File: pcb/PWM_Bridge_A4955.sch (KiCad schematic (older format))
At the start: 18 parts, among them Q3 IPD079N06L3G, Q4 IPD079N06L3G, Q5 IPD079N06L3G, Q6 IPD079N06L3G, U5 A4955GLPTR-T

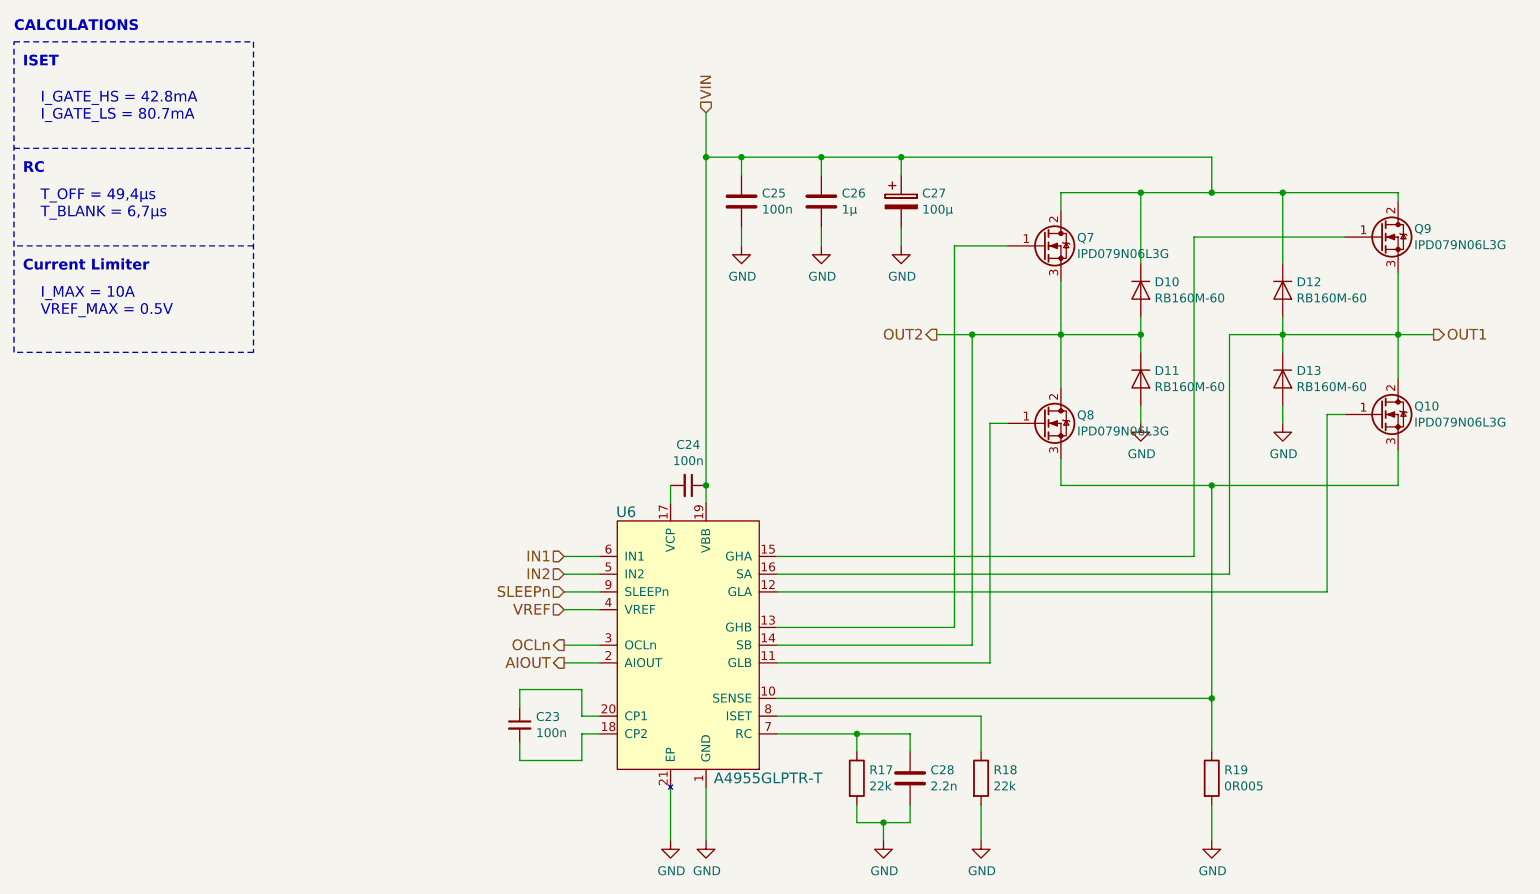
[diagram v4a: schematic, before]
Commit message: Fix little schematic error
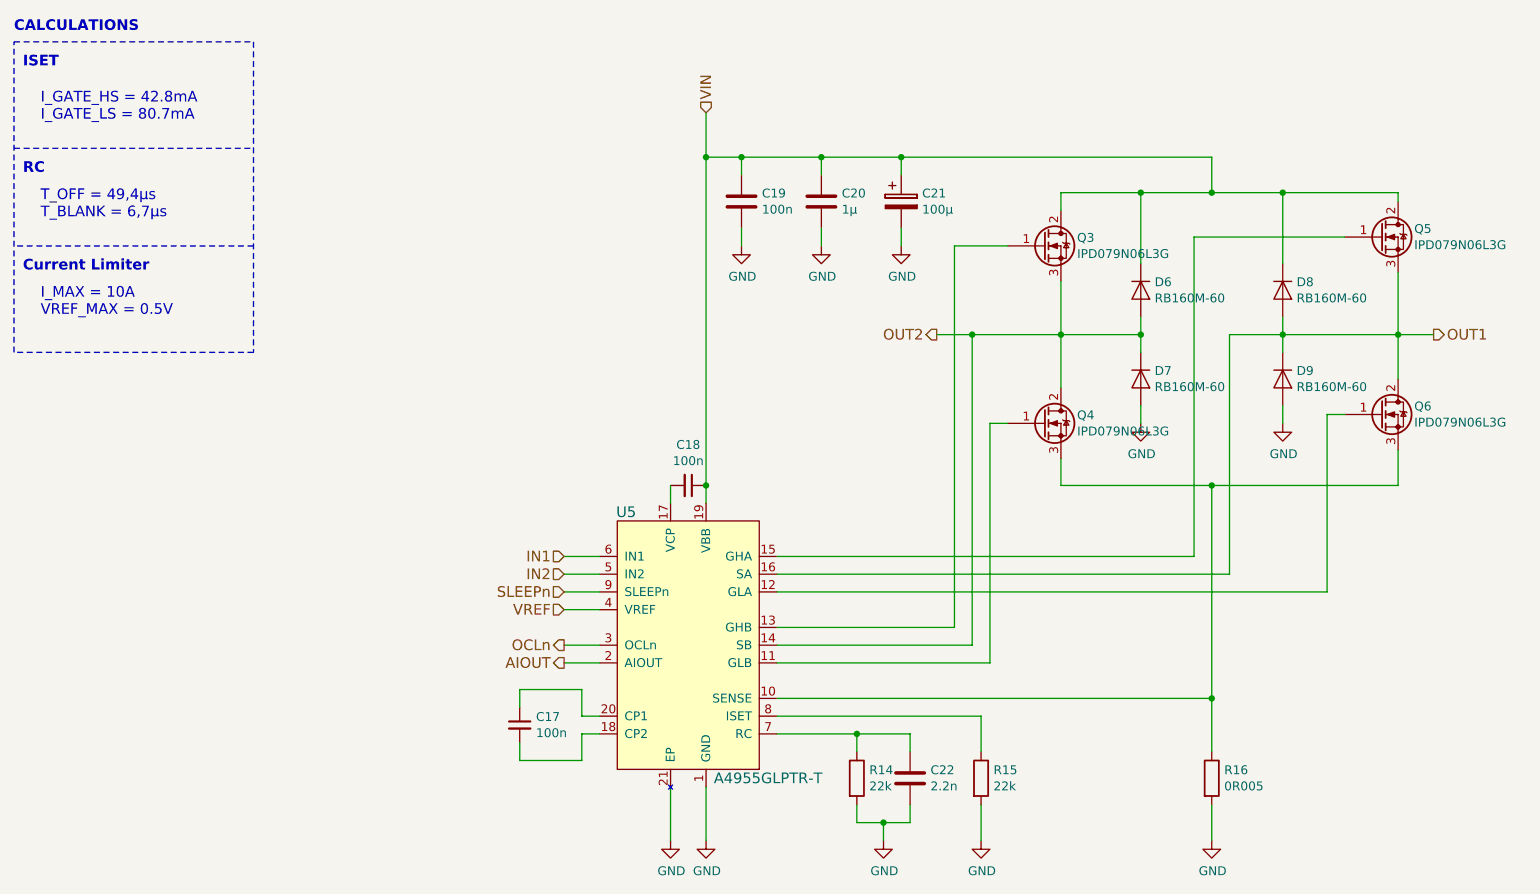
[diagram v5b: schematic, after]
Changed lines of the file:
@@
 AR Path="/58077727/58077F1C" Ref="U5"  Part="1"
 AR Path="/58084D17/58077F1C" Ref="U6"  Part="1"
-F 0 "U6" H 4300 5150 60  0000 C CNN
+F 0 "U5" H 4300 5150 60  0000 C CNN
 F 1 "A4955GLPTR-T" H 5100 3650 60  0000 C CNN
 F 2 "Housings_SSOP:ETSSOP-20-1EP_4.4x6.5mm_Pitch0.65mm" H 4650 4400 60  0001 C CNN
@@
 AR Path="/58077727/5807829A" Ref="C18"  Part="1"
 AR Path="/58084D17/5807829A" Ref="C24"  Part="1"
-F 0 "C24" V 4421 3500 50  0000 C CNN
+F 0 "C18" V 4421 3500 50  0000 C CNN
 F 1 "100n" V 4512 3500 50  0000 C CNN
 F 2 "Capacitors_SMD:C_0603" H 4650 3500 50  0001 C CNN
@@
 AR Path="/58077727/58078520" Ref="R14"  Part="1"
 AR Path="/58084D17/58078520" Ref="R17"  Part="1"
-F 0 "R17" H 5670 5196 50  0000 L CNN
+F 0 "R14" H 5670 5196 50  0000 L CNN
 F 1 "22k" H 5670 5105 50  0000 L CNN
 F 2 "Resistors_SMD:R_0603" V 5530 5150 50  0001 C CNN
@@
 AR Path="/58077727/5807867B" Ref="C22"  Part="1"
 AR Path="/58084D17/5807867B" Ref="C28"  Part="1"
-F 0 "C28" H 6015 5196 50  0000 L CNN
+F 0 "C22" H 6015 5196 50  0000 L CNN
 F 1 "2.2n" H 6015 5105 50  0000 L CNN
 F 2 "Capacitors_SMD:C_0603" H 5938 5000 50  0001 C CNN
@@
 AR Path="/58077727/580787DB" Ref="#PWR070"  Part="1"
 AR Path="/58084D17/580787DB" Ref="#PWR080"  Part="1"
-F 0 "#PWR080" H 5750 5250 50  0001 C CNN
+F 0 "#PWR070" H 5750 5250 50  0001 C CNN
 F 1 "GND" H 5755 5327 50  0000 C CNN
 F 2 "" H 5750 5500 50  0000 C CNN
@@
 AR Path="/58077727/58078835" Ref="#PWR071"  Part="1"
 AR Path="/58084D17/58078835" Ref="#PWR081"  Part="1"
-F 0 "#PWR081" H 4750 5250 50  0001 C CNN
+F 0 "#PWR071" H 4750 5250 50  0001 C CNN
 F 1 "GND" H 4755 5327 50  0000 C CNN
 F 2 "" H 4750 5500 50  0000 C CNN
@@
 AR Path="/58077727/580789CE" Ref="R16"  Part="1"
 AR Path="/58084D17/580789CE" Ref="R19"  Part="1"
-F 0 "R19" H 7670 5196 50  0000 L CNN
+F 0 "R16" H 7670 5196 50  0000 L CNN
 F 1 "0R005" H 7670 5105 50  0000 L CNN
 F 2 "Resistors_SMD:R_2512" V 7530 5150 50  0001 C CNN
@@
 AR Path="/58077727/58078AB1" Ref="#PWR072"  Part="1"
 AR Path="/58084D17/58078AB1" Ref="#PWR082"  Part="1"
-F 0 "#PWR082" H 7600 5250 50  0001 C CNN
+F 0 "#PWR072" H 7600 5250 50  0001 C CNN
 F 1 "GND" H 7605 5327 50  0000 C CNN
 F 2 "" H 7600 5500 50  0000 C CNN
@@
 AR Path="/58077727/58078C46" Ref="Q3"  Part="1"
 AR Path="/58084D17/58078C46" Ref="Q7"  Part="1"
-F 0 "Q7" H 6841 2196 50  0000 L CNN
+F 0 "Q3" H 6841 2196 50  0000 L CNN
 F 1 "IPD079N06L3G" H 6841 2105 50  0000 L CNN
 F 2 "TO_SOT_Packages_SMD_local:PG-TO-252-3-313" H 6850 2250 50  0001 C CNN
@@
 AR Path="/58077727/58078E80" Ref="Q5"  Part="1"
 AR Path="/58084D17/58078E80" Ref="Q9"  Part="1"
-F 0 "Q9" H 8741 2146 50  0000 L CNN
+F 0 "Q5" H 8741 2146 50  0000 L CNN
 F 1 "IPD079N06L3G" H 8741 2055 50  0000 L CNN
 F 2 "TO_SOT_Packages_SMD_local:PG-TO-252-3-313" H 8750 2200 50  0001 C CNN
@@
 AR Path="/58077727/58078ED9" Ref="Q6"  Part="1"
 AR Path="/58084D17/58078ED9" Ref="Q10"  Part="1"
-F 0 "Q10" H 8741 3146 50  0000 L CNN
+F 0 "Q6" H 8741 3146 50  0000 L CNN
 F 1 "IPD079N06L3G" H 8741 3055 50  0000 L CNN
 F 2 "TO_SOT_Packages_SMD_local:PG-TO-252-3-313" H 8750 3200 50  0001 C CNN
@@
 AR Path="/58077727/58078F3F" Ref="Q4"  Part="1"
 AR Path="/58084D17/58078F3F" Ref="Q8"  Part="1"
-F 0 "Q8" H 6841 3196 50  0000 L CNN
+F 0 "Q4" H 6841 3196 50  0000 L CNN
 F 1 "IPD079N06L3G" H 6841 3105 50  0000 L CNN
 F 2 "TO_SOT_Packages_SMD_local:PG-TO-252-3-313" H 6850 3250 50  0001 C CNN
@@
 AR Path="/58077727/5807A394" Ref="C19"  Part="1"
 AR Path="/58084D17/5807A394" Ref="C25"  Part="1"
-F 0 "C25" H 5065 1946 50  0000 L CNN
+F 0 "C19" H 5065 1946 50  0000 L CNN
 F 1 "100n" H 5065 1855 50  0000 L CNN
 F 2 "Capacitors_SMD:C_0603" H 4988 1750 50  0001 C CNN
@@
 AR Path="/58077727/5807A4C6" Ref="#PWR073"  Part="1"
 AR Path="/58084D17/5807A4C6" Ref="#PWR083"  Part="1"
-F 0 "#PWR083" H 4950 1900 50  0001 C CNN
+F 0 "#PWR073" H 4950 1900 50  0001 C CNN
 F 1 "GND" H 4955 1977 50  0000 C CNN
 F 2 "" H 4950 2150 50  0000 C CNN
@@
 AR Path="/58077727/5807A62E" Ref="C21"  Part="1"
 AR Path="/58084D17/5807A62E" Ref="C27"  Part="1"
-F 0 "C27" H 5968 1946 50  0000 L CNN
+F 0 "C21" H 5968 1946 50  0000 L CNN
 F 1 "100µ" H 5968 1855 50  0000 L CNN
 F 2 "Capacitors_SMD:c_elec_10x10" H 5888 1750 50  0001 C CNN
@@
 AR Path="/58077727/5807A964" Ref="#PWR074"  Part="1"
 AR Path="/58084D17/5807A964" Ref="#PWR084"  Part="1"
-F 0 "#PWR084" H 5850 1900 50  0001 C CNN
+F 0 "#PWR074" H 5850 1900 50  0001 C CNN
 F 1 "GND" H 5855 1977 50  0000 C CNN
 F 2 "" H 5850 2150 50  0000 C CNN
@@
 AR Path="/58077727/5807BEA4" Ref="C17"  Part="1"
 AR Path="/58084D17/5807BEA4" Ref="C23"  Part="1"
-F 0 "C23" H 3792 4896 50  0000 L CNN
+F 0 "C17" H 3792 4896 50  0000 L CNN
 F 1 "100n" H 3792 4805 50  0000 L CNN
 F 2 "Capacitors_SMD:C_0603" H 3700 4850 50  0001 C CNN
@@
 AR Path="/58077727/5809AC71" Ref="C20"  Part="1"
 AR Path="/58084D17/5809AC71" Ref="C26"  Part="1"
-F 0 "C26" H 5515 1946 50  0000 L CNN
+F 0 "C20" H 5515 1946 50  0000 L CNN
 F 1 "1µ" H 5515 1855 50  0000 L CNN
 F 2 "Capacitors_SMD:C_0603" H 5438 1750 50  0001 C CNN
@@
 AR Path="/58084D17/5809ACB6" Ref="#PWR085"  Part="1"
 AR Path="/58077727/5809ACB6" Ref="#PWR075"  Part="1"
-F 0 "#PWR085" H 5400 1900 50  0001 C CNN
+F 0 "#PWR075" H 5400 1900 50  0001 C CNN
 F 1 "GND" H 5405 1977 50  0000 C CNN
 F 2 "" H 5400 2150 50  0000 C CNN
@@
 AR Path="/58077727/580A461C" Ref="R15"  Part="1"
 AR Path="/58084D17/580A461C" Ref="R18"  Part="1"
-F 0 "R18" H 6370 5196 50  0000 L CNN
+F 0 "R15" H 6370 5196 50  0000 L CNN
 F 1 "22k" H 6370 5105 50  0000 L CNN
 F 2 "Resistors_SMD:R_0603" V 6230 5150 50  0001 C CNN
@@
 AR Path="/58077727/580A46B3" Ref="#PWR076"  Part="1"
 AR Path="/58084D17/580A46B3" Ref="#PWR086"  Part="1"
-F 0 "#PWR086" H 6300 5250 50  0001 C CNN
+F 0 "#PWR076" H 6300 5250 50  0001 C CNN
 F 1 "GND" H 6305 5327 50  0000 C CNN
 F 2 "" H 6300 5500 50  0000 C CNN
@@
 AR Path="/58077727/58151ECD" Ref="D6"  Part="1"
 AR Path="/58084D17/58151ECD" Ref="D10"  Part="1"
-F 0 "D10" V 7154 2478 50  0000 L CNN
+F 0 "D6" V 7154 2478 50  0000 L CNN
 F 1 "RB160M-60" V 7245 2478 50  0000 L CNN
 F 2 "Diodes_SMD:SOD-123" V 7291 2478 50  0001 L CNN
@@
 AR Path="/58077727/581537FD" Ref="D7"  Part="1"
 AR Path="/58084D17/581537FD" Ref="D11"  Part="1"
-F 0 "D11" V 7154 2978 50  0000 L CNN
+F 0 "D7" V 7154 2978 50  0000 L CNN
 F 1 "RB160M-60" V 7245 2978 50  0000 L CNN
 F 2 "Diodes_SMD:SOD-123" V 7291 2978 50  0001 L CNN
@@
 AR Path="/58077727/58153EBB" Ref="D9"  Part="1"
 AR Path="/58084D17/58153EBB" Ref="D13"  Part="1"
-F 0 "D13" V 7954 2978 50  0000 L CNN
+F 0 "D9" V 7954 2978 50  0000 L CNN
 F 1 "RB160M-60" V 8045 2978 50  0000 L CNN
 F 2 "Diodes_SMD:SOD-123" V 8091 2978 50  0001 L CNN
@@
 AR Path="/58077727/58153F12" Ref="D8"  Part="1"
 AR Path="/58084D17/58153F12" Ref="D12"  Part="1"
-F 0 "D12" V 7954 2478 50  0000 L CNN
+F 0 "D8" V 7954 2478 50  0000 L CNN
 F 1 "RB160M-60" V 8045 2478 50  0000 L CNN
 F 2 "Diodes_SMD:SOD-123" V 8091 2478 50  0001 L CNN
@@
 AR Path="/58077727/581550B7" Ref="#PWR077"  Part="1"
 AR Path="/58084D17/581550B7" Ref="#PWR087"  Part="1"
-F 0 "#PWR087" H 8000 2900 50  0001 C CNN
+F 0 "#PWR077" H 8000 2900 50  0001 C CNN
 F 1 "GND" H 8005 2977 50  0000 C CNN
 F 2 "" H 8000 3150 50  0000 C CNN
@@
 AR Path="/58077727/58155164" Ref="#PWR078"  Part="1"
 AR Path="/58084D17/58155164" Ref="#PWR088"  Part="1"
-F 0 "#PWR088" H 7200 2900 50  0001 C CNN
+F 0 "#PWR078" H 7200 2900 50  0001 C CNN
 F 1 "GND" H 7205 2977 50  0000 C CNN
 F 2 "" H 7200 3150 50  0000 C CNN
@@
 AR Path="/58077727/582EE915" Ref="#PWR079"  Part="1"
 AR Path="/58084D17/582EE915" Ref="#PWR089"  Part="1"
-F 0 "#PWR089" H 4550 5250 50  0001 C CNN
+F 0 "#PWR079" H 4550 5250 50  0001 C CNN
 F 1 "GND" H 4555 5327 50  0000 C CNN
 F 2 "" H 4550 5500 50  0000 C CNN

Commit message: Improve pcb layout
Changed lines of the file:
@@
 AR Path="/58077727/58077F1C" Ref="U5"  Part="1"
 AR Path="/58084D17/58077F1C" Ref="U6"  Part="1"
-F 0 "U5" H 4300 5150 60  0000 C CNN
+F 0 "U6" H 4300 5150 60  0000 C CNN
 F 1 "A4955GLPTR-T" H 5100 3650 60  0000 C CNN
 F 2 "Housings_SSOP:ETSSOP-20-1EP_4.4x6.5mm_Pitch0.65mm" H 4650 4400 60  0001 C CNN
@@
 AR Path="/58077727/5807829A" Ref="C18"  Part="1"
 AR Path="/58084D17/5807829A" Ref="C24"  Part="1"
-F 0 "C18" V 4421 3500 50  0000 C CNN
+F 0 "C24" V 4421 3500 50  0000 C CNN
 F 1 "100n" V 4512 3500 50  0000 C CNN
 F 2 "Capacitors_SMD:C_0603" H 4650 3500 50  0001 C CNN
@@
 AR Path="/58077727/58078520" Ref="R14"  Part="1"
 AR Path="/58084D17/58078520" Ref="R17"  Part="1"
-F 0 "R14" H 5670 5196 50  0000 L CNN
+F 0 "R17" H 5670 5196 50  0000 L CNN
 F 1 "22k" H 5670 5105 50  0000 L CNN
 F 2 "Resistors_SMD:R_0603" V 5530 5150 50  0001 C CNN
@@
 AR Path="/58077727/5807867B" Ref="C22"  Part="1"
 AR Path="/58084D17/5807867B" Ref="C28"  Part="1"
-F 0 "C22" H 6015 5196 50  0000 L CNN
+F 0 "C28" H 6015 5196 50  0000 L CNN
 F 1 "2.2n" H 6015 5105 50  0000 L CNN
 F 2 "Capacitors_SMD:C_0603" H 5938 5000 50  0001 C CNN
@@
 AR Path="/58077727/580789CE" Ref="R16"  Part="1"
 AR Path="/58084D17/580789CE" Ref="R19"  Part="1"
-F 0 "R16" H 7670 5196 50  0000 L CNN
+F 0 "R19" H 7670 5196 50  0000 L CNN
 F 1 "0R005" H 7670 5105 50  0000 L CNN
 F 2 "Resistors_SMD:R_2512" V 7530 5150 50  0001 C CNN
@@
 AR Path="/58077727/58078C46" Ref="Q3"  Part="1"
 AR Path="/58084D17/58078C46" Ref="Q7"  Part="1"
-F 0 "Q3" H 6841 2196 50  0000 L CNN
+F 0 "Q7" H 6841 2196 50  0000 L CNN
 F 1 "IPD079N06L3G" H 6841 2105 50  0000 L CNN
 F 2 "TO_SOT_Packages_SMD_local:PG-TO-252-3-313" H 6850 2250 50  0001 C CNN
@@
 AR Path="/58077727/58078E80" Ref="Q5"  Part="1"
 AR Path="/58084D17/58078E80" Ref="Q9"  Part="1"
-F 0 "Q5" H 8741 2146 50  0000 L CNN
+F 0 "Q9" H 8741 2146 50  0000 L CNN
 F 1 "IPD079N06L3G" H 8741 2055 50  0000 L CNN
 F 2 "TO_SOT_Packages_SMD_local:PG-TO-252-3-313" H 8750 2200 50  0001 C CNN
@@
 AR Path="/58077727/58078ED9" Ref="Q6"  Part="1"
 AR Path="/58084D17/58078ED9" Ref="Q10"  Part="1"
-F 0 "Q6" H 8741 3146 50  0000 L CNN
+F 0 "Q10" H 8741 3146 50  0000 L CNN
 F 1 "IPD079N06L3G" H 8741 3055 50  0000 L CNN
 F 2 "TO_SOT_Packages_SMD_local:PG-TO-252-3-313" H 8750 3200 50  0001 C CNN
@@
 AR Path="/58077727/58078F3F" Ref="Q4"  Part="1"
 AR Path="/58084D17/58078F3F" Ref="Q8"  Part="1"
-F 0 "Q4" H 6841 3196 50  0000 L CNN
+F 0 "Q8" H 6841 3196 50  0000 L CNN
 F 1 "IPD079N06L3G" H 6841 3105 50  0000 L CNN
 F 2 "TO_SOT_Packages_SMD_local:PG-TO-252-3-313" H 6850 3250 50  0001 C CNN
@@
 AR Path="/58077727/5807A394" Ref="C19"  Part="1"
 AR Path="/58084D17/5807A394" Ref="C25"  Part="1"
-F 0 "C19" H 5065 1946 50  0000 L CNN
+F 0 "C25" H 5065 1946 50  0000 L CNN
 F 1 "100n" H 5065 1855 50  0000 L CNN
 F 2 "Capacitors_SMD:C_0603" H 4988 1750 50  0001 C CNN
@@
 AR Path="/58077727/5807A62E" Ref="C21"  Part="1"
 AR Path="/58084D17/5807A62E" Ref="C27"  Part="1"
-F 0 "C21" H 5968 1946 50  0000 L CNN
+F 0 "C27" H 5968 1946 50  0000 L CNN
 F 1 "100µ" H 5968 1855 50  0000 L CNN
 F 2 "Capacitors_SMD:c_elec_10x10" H 5888 1750 50  0001 C CNN
@@
 AR Path="/58077727/5807BEA4" Ref="C17"  Part="1"
 AR Path="/58084D17/5807BEA4" Ref="C23"  Part="1"
-F 0 "C17" H 3792 4896 50  0000 L CNN
+F 0 "C23" H 3792 4896 50  0000 L CNN
 F 1 "100n" H 3792 4805 50  0000 L CNN
 F 2 "Capacitors_SMD:C_0603" H 3700 4850 50  0001 C CNN
@@
 AR Path="/58077727/5809AC71" Ref="C20"  Part="1"
 AR Path="/58084D17/5809AC71" Ref="C26"  Part="1"
-F 0 "C20" H 5515 1946 50  0000 L CNN
+F 0 "C26" H 5515 1946 50  0000 L CNN
 F 1 "1µ" H 5515 1855 50  0000 L CNN
 F 2 "Capacitors_SMD:C_0603" H 5438 1750 50  0001 C CNN
@@
 AR Path="/58077727/580A461C" Ref="R15"  Part="1"
 AR Path="/58084D17/580A461C" Ref="R18"  Part="1"
-F 0 "R15" H 6370 5196 50  0000 L CNN
+F 0 "R18" H 6370 5196 50  0000 L CNN
 F 1 "22k" H 6370 5105 50  0000 L CNN
 F 2 "Resistors_SMD:R_0603" V 6230 5150 50  0001 C CNN
@@
 AR Path="/58077727/58151ECD" Ref="D6"  Part="1"
 AR Path="/58084D17/58151ECD" Ref="D10"  Part="1"
-F 0 "D6" V 7154 2478 50  0000 L CNN
+F 0 "D10" V 7154 2478 50  0000 L CNN
 F 1 "RB160M-60" V 7245 2478 50  0000 L CNN
 F 2 "Diodes_SMD:SOD-123" V 7291 2478 50  0001 L CNN
@@
 AR Path="/58077727/581537FD" Ref="D7"  Part="1"
 AR Path="/58084D17/581537FD" Ref="D11"  Part="1"
-F 0 "D7" V 7154 2978 50  0000 L CNN
+F 0 "D11" V 7154 2978 50  0000 L CNN
 F 1 "RB160M-60" V 7245 2978 50  0000 L CNN
 F 2 "Diodes_SMD:SOD-123" V 7291 2978 50  0001 L CNN
@@
 AR Path="/58077727/58153EBB" Ref="D9"  Part="1"
 AR Path="/58084D17/58153EBB" Ref="D13"  Part="1"
-F 0 "D9" V 7954 2978 50  0000 L CNN
+F 0 "D13" V 7954 2978 50  0000 L CNN
 F 1 "RB160M-60" V 8045 2978 50  0000 L CNN
 F 2 "Diodes_SMD:SOD-123" V 8091 2978 50  0001 L CNN
@@
 AR Path="/58077727/58153F12" Ref="D8"  Part="1"
 AR Path="/58084D17/58153F12" Ref="D12"  Part="1"
-F 0 "D8" V 7954 2478 50  0000 L CNN
+F 0 "D12" V 7954 2478 50  0000 L CNN
 F 1 "RB160M-60" V 8045 2478 50  0000 L CNN
 F 2 "Diodes_SMD:SOD-123" V 8091 2478 50  0001 L CNN
